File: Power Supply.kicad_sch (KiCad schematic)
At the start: 12 parts, among them J4 Conn_01x04, J6 Conn_01x03, T1A Transformer_1P_SS, T1B Transformer_1P_SS

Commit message: Label connectors in PSU
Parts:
- J4: value Conn_01x04 -> Logic Board
- J6: value Conn_01x03 -> RF Terminal Strip
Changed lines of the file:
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@@
       (effects (font (size 1.27 1.27)) (justify left))
     )
-    (property "Value" "Conn_01x03" (at 198.12 93.345 0)
+    (property "Value" "RF Terminal Strip" (at 198.12 93.345 0)
       (effects (font (size 1.27 1.27)) (justify left))
     )
@@
       (effects (font (size 1.27 1.27)) (justify left))
     )
-    (property "Value" "Conn_01x04" (at 173.99 90.805 0)
+    (property "Value" "Logic Board" (at 173.99 90.805 0)
       (effects (font (size 1.27 1.27)) (justify left))
     )

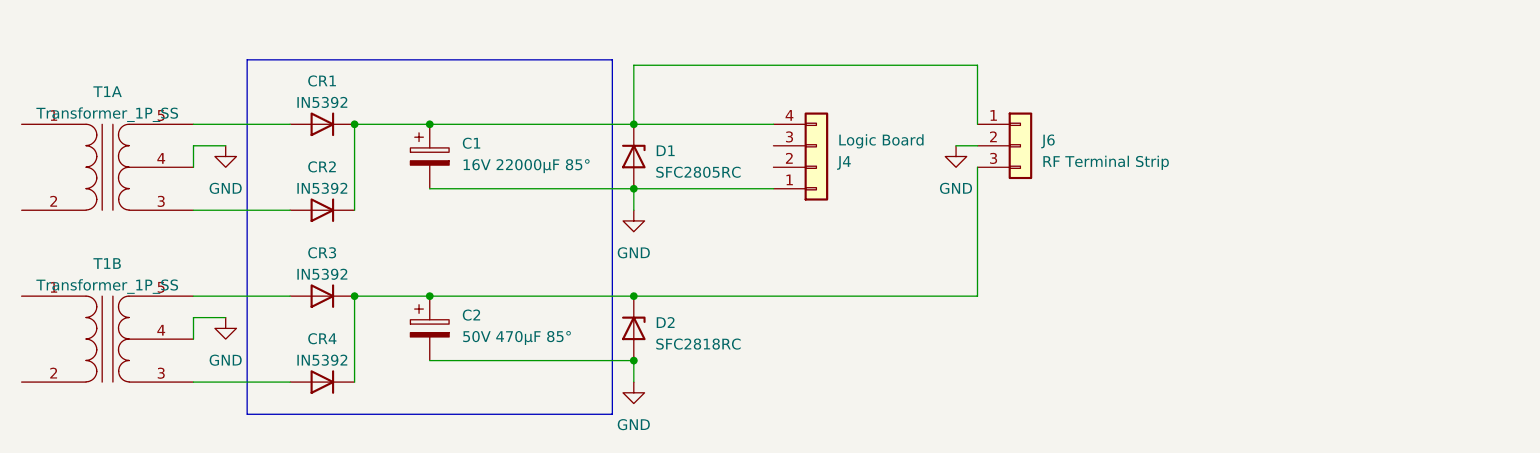
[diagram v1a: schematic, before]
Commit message: Add capacitors on each side of the zeners.
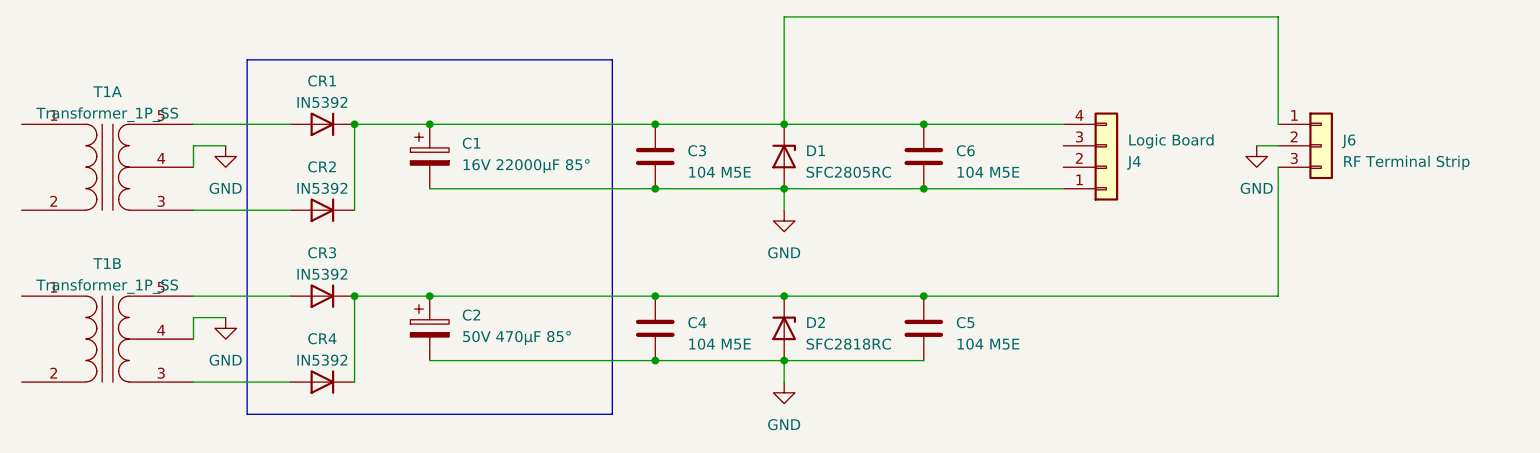
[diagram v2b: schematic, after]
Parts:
- added C3, C4, C5, C6: 104 M5E, symbol Device:C
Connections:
- net GND: now also C3.2, C4.2, C5.2, C6.2
- net at C1.1, CR1.1 (K), CR2.1 (K)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: now also C3.1, C6.1
- net at C2.1, CR3.1 (K), CR4.1 (K)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: now also C4.1, C5.1
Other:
- moved on the sheet: D1, D2, J4, J6
